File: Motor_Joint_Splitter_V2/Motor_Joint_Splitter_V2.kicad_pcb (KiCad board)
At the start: 2 copper layers, 45 x 45 mm, 21 parts, among them J2 26605030, J7 ethernet_54602-908LF, J8 motor_connector_292206-8, J9 Conn_01x05, U2 74ACT244MTCX

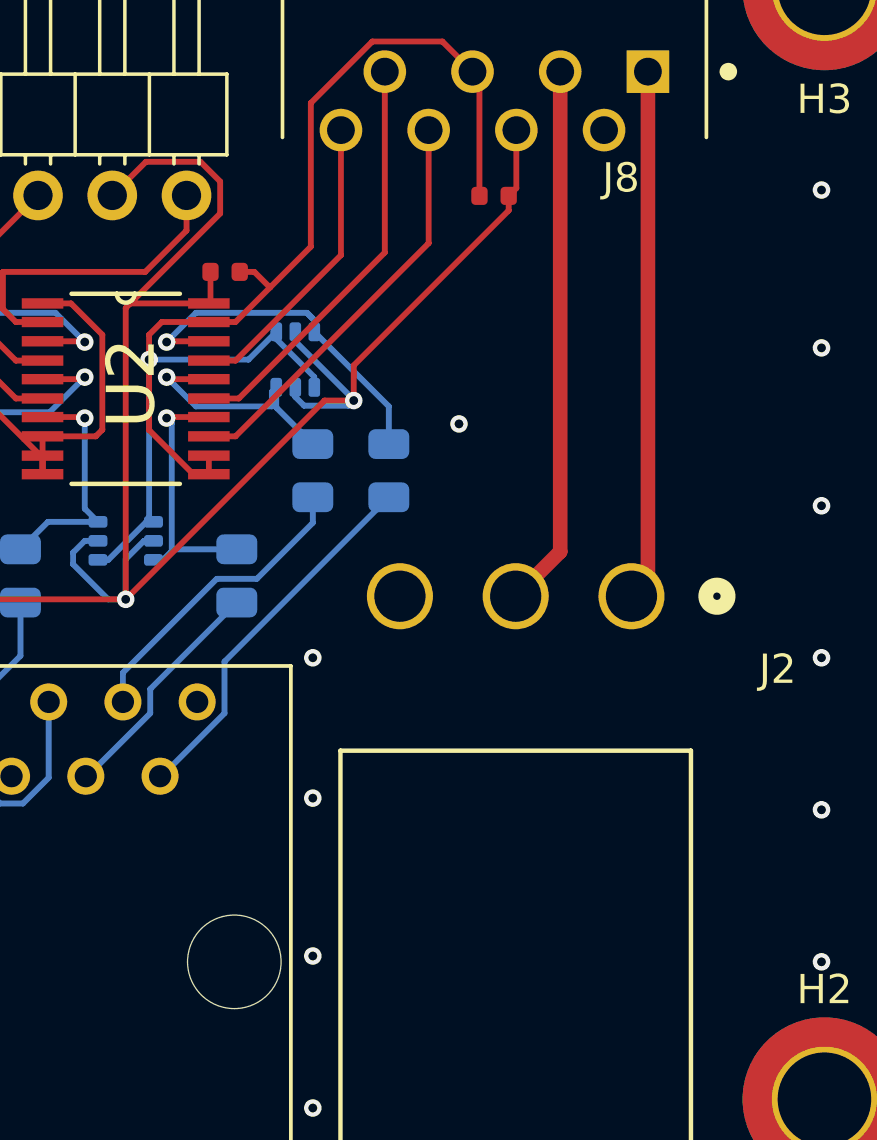
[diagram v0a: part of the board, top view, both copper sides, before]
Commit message: Finalized board, order for it is sitting on JLCPCB's website and everything looks good.
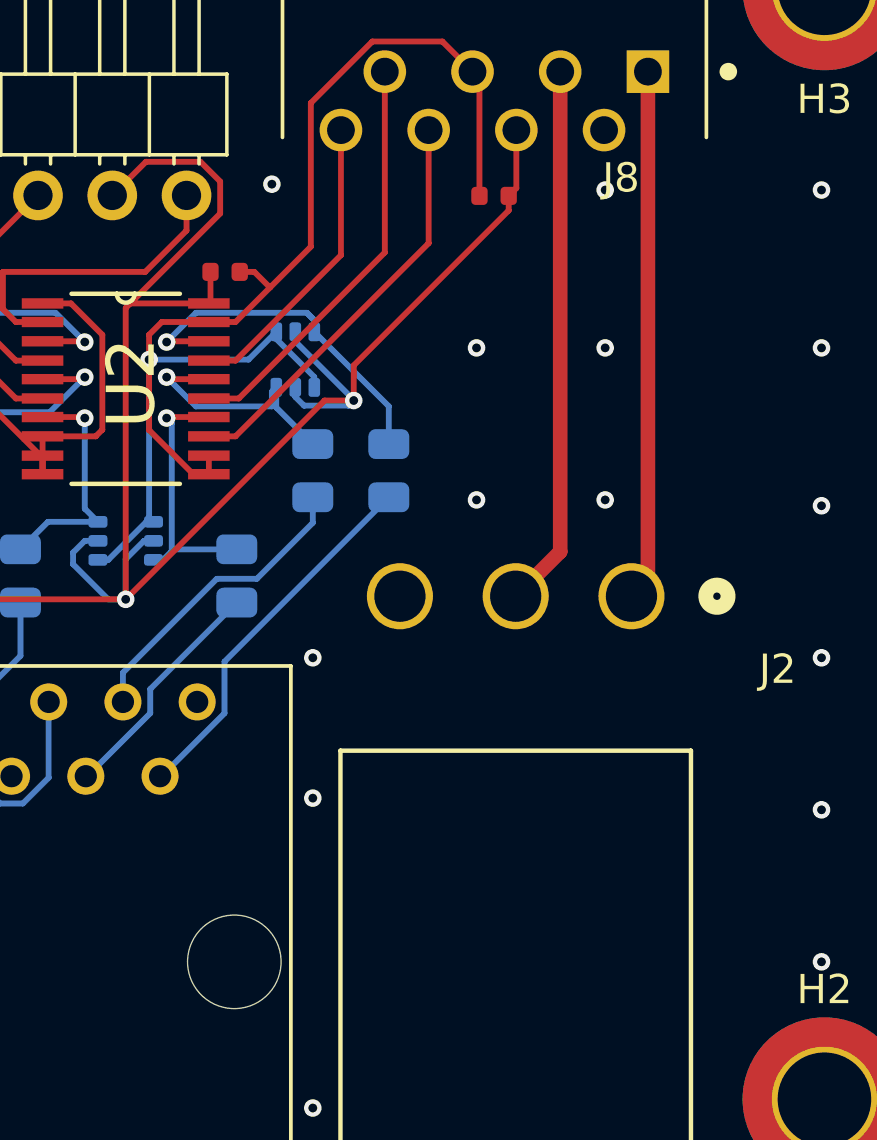
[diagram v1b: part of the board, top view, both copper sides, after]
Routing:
- net GND: vias 21 -> 25
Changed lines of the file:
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@@
 	)
 	(via
-		(at 204 96.6)
+		(at 214 75.8)
 		(size 0.6)
 		(drill 0.3)
@@
 	)
 	(via
+		(at 214 81)
+		(size 0.6)
+		(drill 0.3)
+		(layers "F.Cu" "B.Cu")
+		(free yes)
+		(net 1)
+	)
+	(via
 		(at 221.4 86.4)
 		(size 0.6)
@@
 	)
 	(via
-		(at 209 78.4)
-		(size 0.6)
-		(drill 0.3)
-		(layers "F.Cu" "B.Cu")
-		(free yes)
-		(net 1)
-	)
-	(via
 		(at 198.4 76.2)
 		(size 0.6)
@@
 	)
 	(via
+		(at 202.6 70.2)
+		(size 0.6)
+		(drill 0.3)
+		(layers "F.Cu" "B.Cu")
+		(free yes)
+		(net 1)
+	)
+	(via
 		(at 183.8 91.4)
 		(size 0.6)
@@
 	)
 	(via
+		(at 214 70.4)
+		(size 0.6)
+		(drill 0.3)
+		(layers "F.Cu" "B.Cu")
+		(free yes)
+		(net 1)
+	)
+	(via
 		(at 185.8 84.4)
 		(size 0.6)
@@
 	)
 	(via
+		(at 209.6 75.8)
+		(size 0.6)
+		(drill 0.3)
+		(layers "F.Cu" "B.Cu")
+		(free yes)
+		(net 1)
+	)
+	(via
 		(at 221.4 70.4)
 		(size 0.6)
@@
 	(via
 		(at 221.4 75.8)
+		(size 0.6)
+		(drill 0.3)
+		(layers "F.Cu" "B.Cu")
+		(free yes)
+		(net 1)
+	)
+	(via
+		(at 209.6 81)
 		(size 0.6)
 		(drill 0.3)
@@
 		(priority 1)
 		(connect_pads
-			(clearance 2)
+			(clearance 0.5)
 		)
 		(min_thickness 0.25)

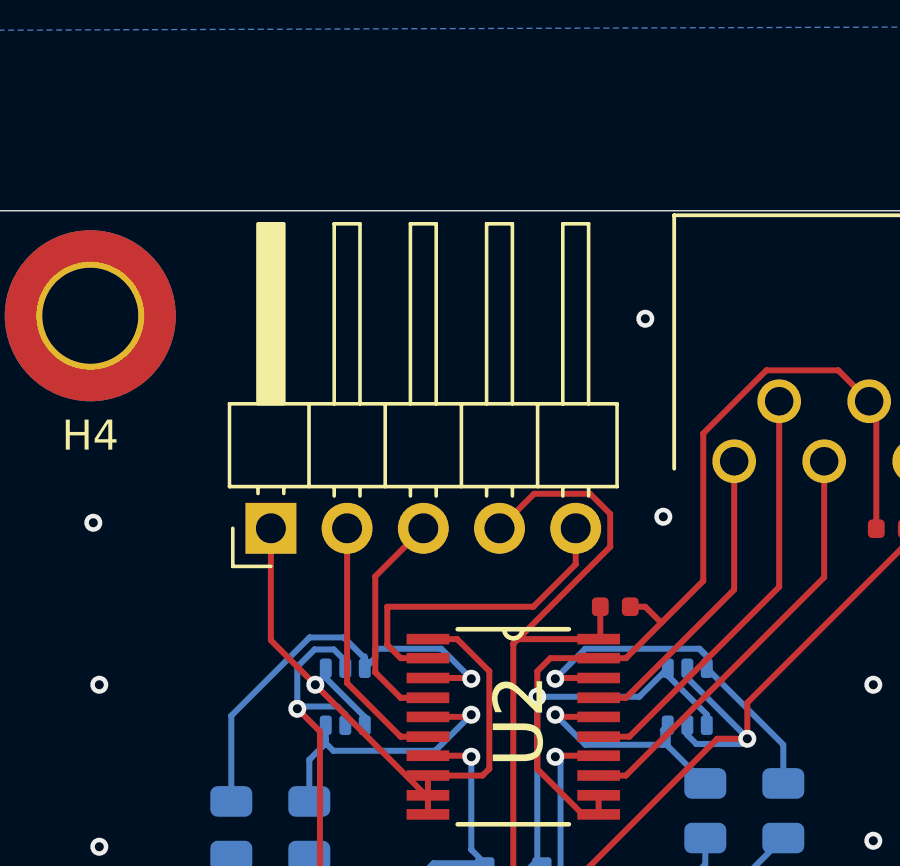
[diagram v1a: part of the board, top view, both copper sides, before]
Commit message: Added changes for shifting the SEA encoder connector's pins to extend slightly off the board to avoid collision with the cable assembly.
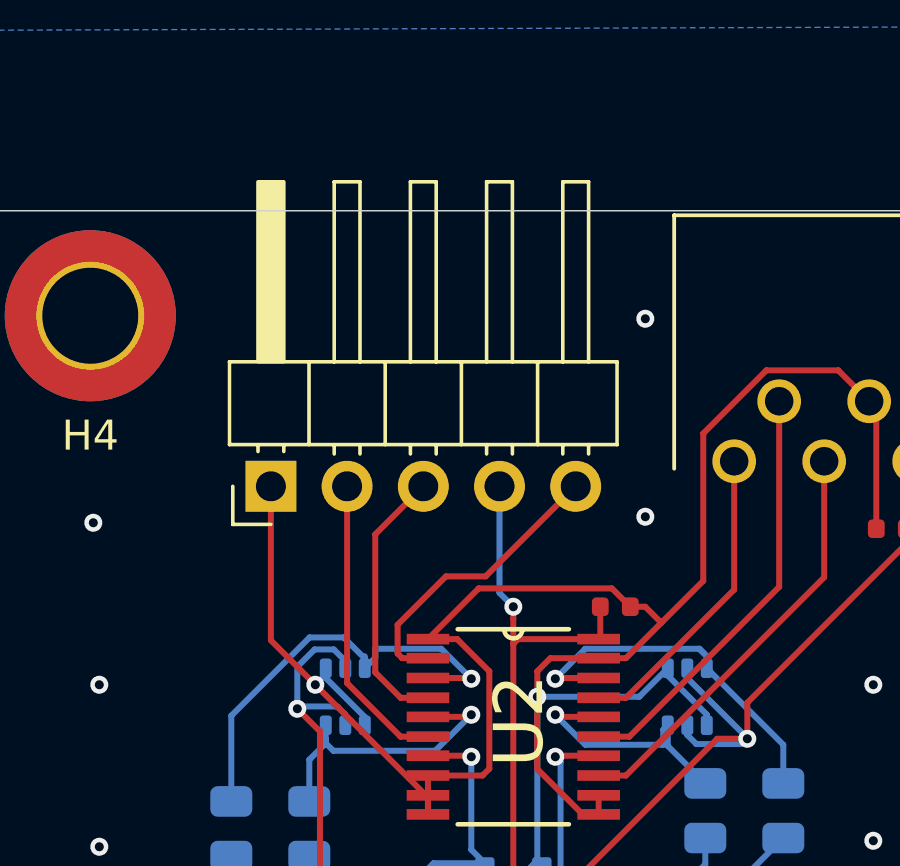
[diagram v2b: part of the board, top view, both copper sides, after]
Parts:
- moved J9 1.40 mm to (189.5, 69.2)
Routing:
- net GND: track 71.5 -> 80.6 mm
- net +5V: track 86.3 -> 81.9 mm, vias 3 -> 4
- net /SEA_A: track 7.57 -> 8.97 mm
- net /SEA_I: track 8.60 -> 10.00 mm
- net /SEA_B: track 10.9 -> 9.88 mm
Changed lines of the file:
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@@
 	(footprint "Connector_PinHeader_2.54mm:PinHeader_1x05_P2.54mm_Horizontal"
 		(layer "F.Cu")
-		(at 189.52 70.585 90)
+		(at 189.52 69.185 90)
 		(descr "Through hole angled pin header, 1x05, 2.54mm pitch, 6mm pin length, single row")
 		(tags "Through hole angled pin header THT 1x05 2.54mm single row")
@@
 	)
 	(segment
+		(start 189.52 74.32)
+		(end 189.52 69.185)
+		(width 0.2)
+		(layer "F.Cu")
+		(net 1)
+	)
+	(segment
 		(start 198.4 76.2)
 		(end 198.4 75.350057)
@@
 	)
 	(segment
+		(start 201.5 73.2)
+		(end 200.889 72.589)
+		(width 0.2)
+		(layer "F.Cu")
+		(net 1)
+	)
+	(segment
 		(start 202 73.2)
 		(end 202.535 73.735)
@@
 	)
 	(segment
+		(start 191 75.8)
+		(end 189.52 74.32)
+		(width 0.2)
+		(layer "F.Cu")
+		(net 1)
+	)
+	(segment
 		(start 194.7552 80.121)
 		(end 194.7552 79.5552)
@@
 	)
 	(segment
-		(start 189.52 74.32)
-		(end 189.52 70.585)
+		(start 200.889 72.589)
+		(end 196.4452 72.589)
 		(width 0.2)
 		(layer "F.Cu")
@@
 	)
 	(segment
-		(start 198.4 75.350057)
-		(end 198.836057 74.914)
+		(start 196.4452 72.589)
+		(end 194.7552 74.279)
 		(width 0.2)
 		(layer "F.Cu")
@@
 	)
 	(segment
-		(start 191 75.8)
-		(end 189.52 74.32)
+		(start 198.4 75.350057)
+		(end 198.836057 74.914)
 		(width 0.2)
 		(layer "F.Cu")
@@
 	)
 	(via
-		(at 202.6 70.2)
+		(at 202 70.2)
 		(size 0.6)
 		(drill 0.3)
@@
 	)
 	(segment
-		(start 200.831 71.203181)
-		(end 200.831 70.10824)
-		(width 0.2)
-		(layer "F.Cu")
-		(net 4)
-	)
-	(segment
 		(start 191.155 90.45)
 		(end 191.155 84.4)
@@
 	)
 	(segment
-		(start 191.155 77.355)
-		(end 190.4 76.6)
+		(start 200.5 73.2)
+		(end 200.4 73.2)
 		(width 0.2)
 		(layer "F.Cu")
@@
 	)
 	(segment
-		(start 197.755181 74.279)
-		(end 200.831 71.203181)
+		(start 191.155 77.355)
+		(end 190.4 76.6)
 		(width 0.2)
 		(layer "F.Cu")
@@
 	)
 	(segment
-		(start 197.6 84.4)
-		(end 197.6 74.434181)
+		(start 197.6 73.6)
+		(end 197.6 73.2)
 		(width 0.2)
 		(layer "F.Cu")
@@
 	)
 	(segment
-		(start 200.831 70.10824)
-		(end 200.15676 69.434)
+		(start 197.6 84.4)
+		(end 197.6 74.434181)
 		(width 0.2)
 		(layer "F.Cu")
@@
 	)
 	(segment
-		(start 198.291 69.434)
-		(end 197.14 70.585)
-		(width 0.2)
-		(layer "F.Cu")
-		(net 4)
-	)
-	(segment
 		(start 210.9625 68.35)
 		(end 210.9625 70.3375)
@@
 	)
 	(segment
-		(start 200.4448 74.279)
-		(end 197.755181 74.279)
+		(start 197.6 74.434181)
+		(end 197.6 73.6)
 		(width 0.2)
 		(layer "F.Cu")
@@
 	)
 	(segment
-		(start 200.15676 69.434)
-		(end 198.291 69.434)
+		(start 200.4448 74.279)
+		(end 197.755181 74.279)
 		(width 0.2)
 		(layer "F.Cu")
@@
 	)
 	(via
+		(at 197.6 73.2)
+		(size 0.6)
+		(drill 0.3)
+		(layers "F.Cu" "B.Cu")
+		(net 4)
+	)
+	(via
 		(at 205.4 77.6)
 		(size 0.6)
@@
 	)
 	(segment
+		(start 197.14 72.74)
+		(end 197.14 69.185)
+		(width 0.2)
+		(layer "B.Cu")
+		(net 4)
+	)
+	(segment
 		(start 190.4 76.6)
 		(end 190.4 75.2)
@@
 	)
 	(segment
+		(start 197.6 73.2)
+		(end 197.14 72.74)
+		(width 0.2)
+		(layer "B.Cu")
+		(net 4)
+	)
+	(segment
 		(start 190.4 75.2)
 		(end 190.976 74.624)
@@
 	)
 	(segment
-		(start 192.999 72.186)
-		(end 192.999 75.3898)
+		(start 194.6 69.185)
+		(end 192.999 70.786)
 		(width 0.2)
 		(layer "F.Cu")
@@
 	)
 	(segment
-		(start 193.844 76.2348)
-		(end 194.7552 76.2348)
+		(start 192.999 70.786)
+		(end 192.999 75.3898)
 		(width 0.2)
 		(layer "F.Cu")
@@
 	)
 	(segment
-		(start 194.6 70.585)
-		(end 192.999 72.186)
+		(start 193.844 76.2348)
+		(end 194.7552 76.2348)
 		(width 0.2)
 		(layer "F.Cu")
@@
 	)
 	(segment
-		(start 192.06 75.7462)
-		(end 193.844 77.5302)
+		(start 192.06 69.185)
+		(end 192.06 75.7462)
 		(width 0.2)
 		(layer "F.Cu")
@@
 	)
 	(segment
-		(start 192.06 70.585)
-		(end 192.06 75.7462)
+		(start 192.06 75.7462)
+		(end 193.844 77.5302)
 		(width 0.2)
 		(layer "F.Cu")
@@
 	)
 	(segment
-		(start 193.4 74.47)
-		(end 193.844 74.914)
+		(start 195.3552 72.188)
+		(end 196.677 72.188)
 		(width 0.2)
 		(layer "F.Cu")
@@
 	)
 	(segment
-		(start 199.68 71.787081)
-		(end 198.267081 73.2)
+		(start 196.677 72.188)
+		(end 199.68 69.185)
 		(width 0.2)
 		(layer "F.Cu")
@@
 	)
 	(segment
-		(start 193.4 73.2)
-		(end 193.4 74.47)
+		(start 193.8992 74.914)
+		(end 193.743 74.7578)
 		(width 0.2)
 		(layer "F.Cu")
@@
 	)
 	(segment
-		(start 199.68 70.585)
-		(end 199.68 71.787081)
+		(start 193.743 73.8002)
+		(end 195.3552 72.188)
 		(width 0.2)
 		(layer "F.Cu")
@@
 	)
 	(segment
-		(start 193.844 74.914)
-		(end 194.7552 74.914)
+		(start 193.743 74.7578)
+		(end 193.743 73.8002)
 		(width 0.2)
 		(layer "F.Cu")
@@
 	)
 	(segment
-		(start 198.267081 73.2)
-		(end 193.4 73.2)
+		(start 194.7552 74.914)
+		(end 193.8992 74.914)
 		(width 0.2)
 		(layer "F.Cu")
